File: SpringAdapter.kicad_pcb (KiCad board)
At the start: 2 copper layers, 81.7 x 26.6 mm, 50 parts, among them J1 Molex 0472861001, J2 Molex 0472861001, J3 Molex 0472861001, J4 Molex 0472861001, U1 XC6206P332MR-G, U3 GL852G-OHY60_C7501404, X1 12MHz

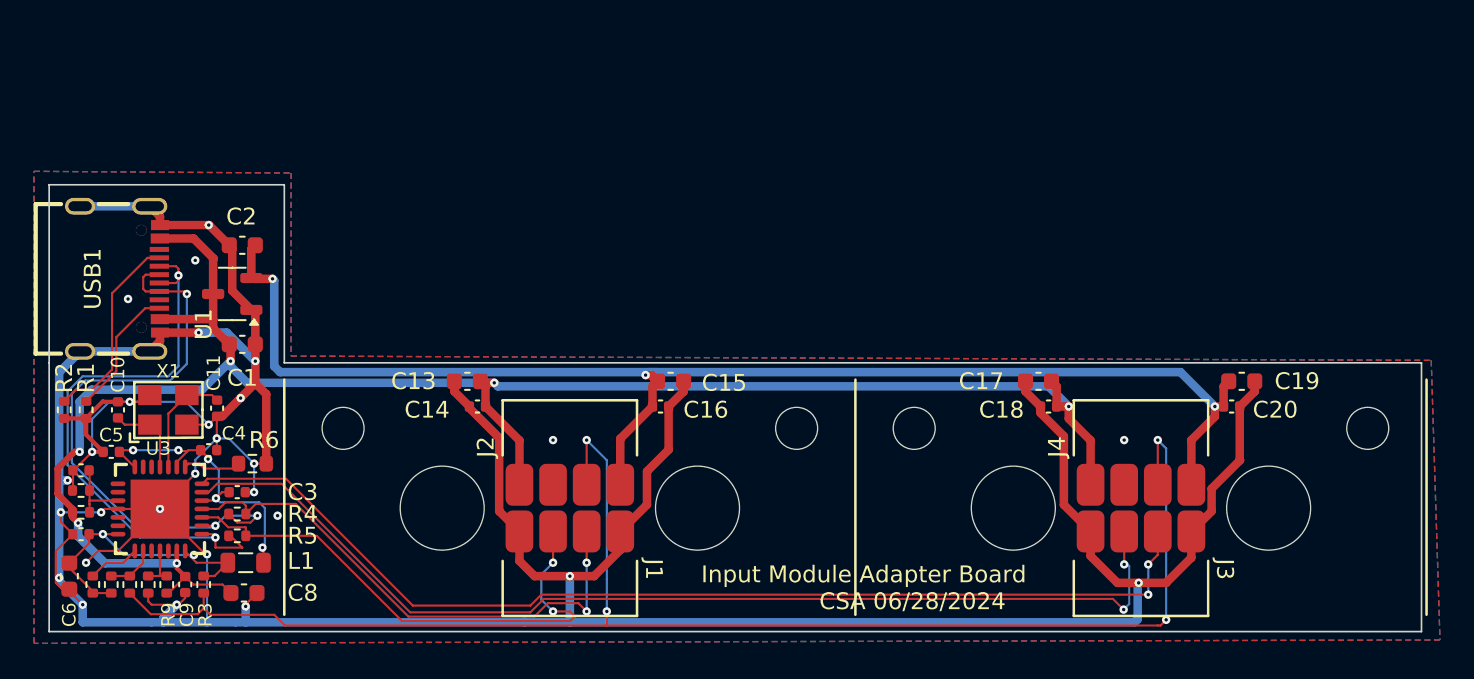
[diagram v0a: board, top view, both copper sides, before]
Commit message: Move USB-C adapter up 1mm
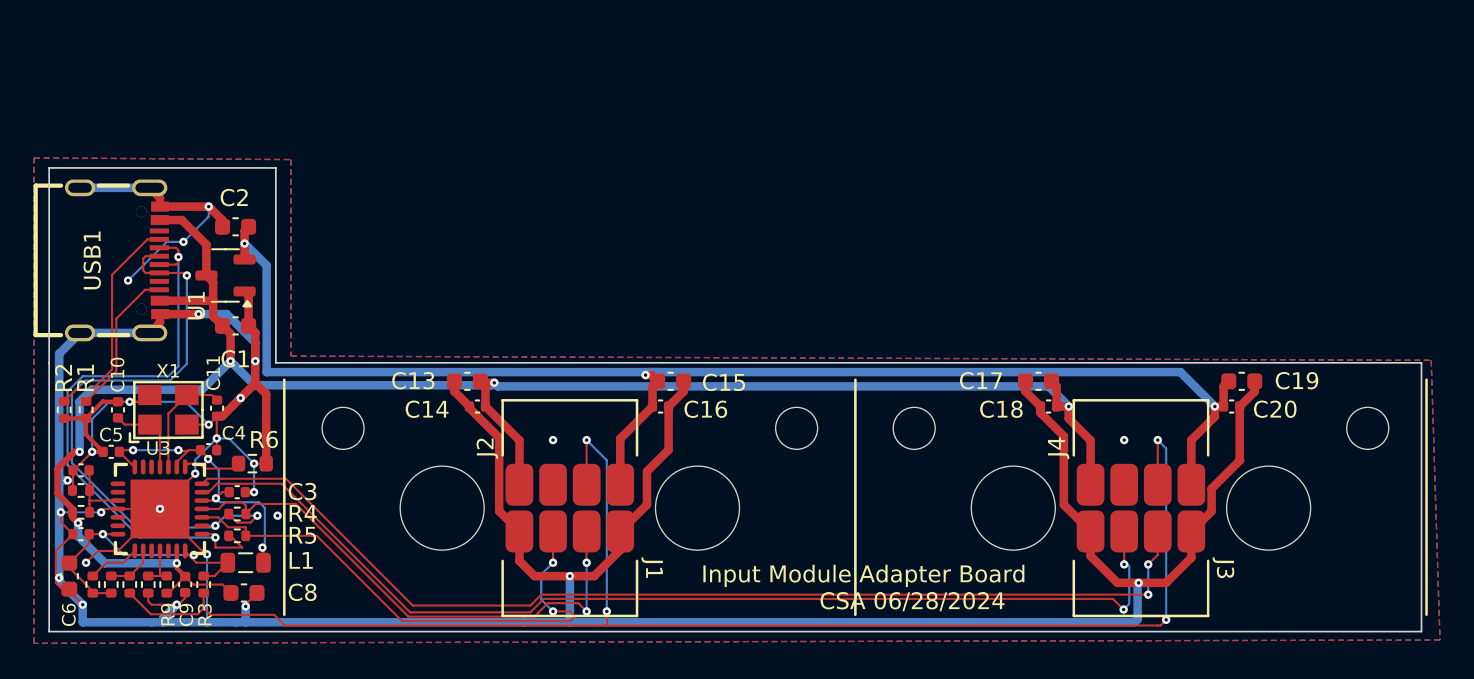
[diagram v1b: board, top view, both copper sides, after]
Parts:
- moved C1 1.17 mm to (96.1, 97.8)
- moved U1 1.17 mm to (95.5, 94.8)
- moved C2 1.17 mm to (96.1, 91.9)
- moved USB1 1.10 mm to (89.2, 93.9)
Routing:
- net GND: track 257.8 -> 263.7 mm
- net +3.3VP: track 81.7 -> 83.6 mm
- net /USB_D_P: track 36.1 -> 37.2 mm
- net /USB_D_N: track 34.9 -> 36.0 mm
- net Net-(USB1-CC1): track 11.9 -> 13.0 mm
- net Net-(USB1-CC2): track 7.84 -> 8.94 mm
- net +5V: track 112.3 -> 112.9 mm
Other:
- board size 81.7 x 26.6 mm -> 81.7 x 27.6 mm

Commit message: DFM work
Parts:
- added H10: Tooling Hole, ExternalMount:JLCPCB Tooling Hole, F.Cu at (86.1, 114.9)
- added H11: Tooling Hole, ExternalMount:JLCPCB Tooling Hole, F.Cu at (165.3, 101.4)
- added H12: Tooling Hole, ExternalMount:JLCPCB Tooling Hole, F.Cu at (165.2, 114.6)
- added H9: Tooling Hole, ExternalMount:JLCPCB Tooling Hole, F.Cu at (97.0, 89.8)
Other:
- board text added: "JLCJLCJLCJLC"

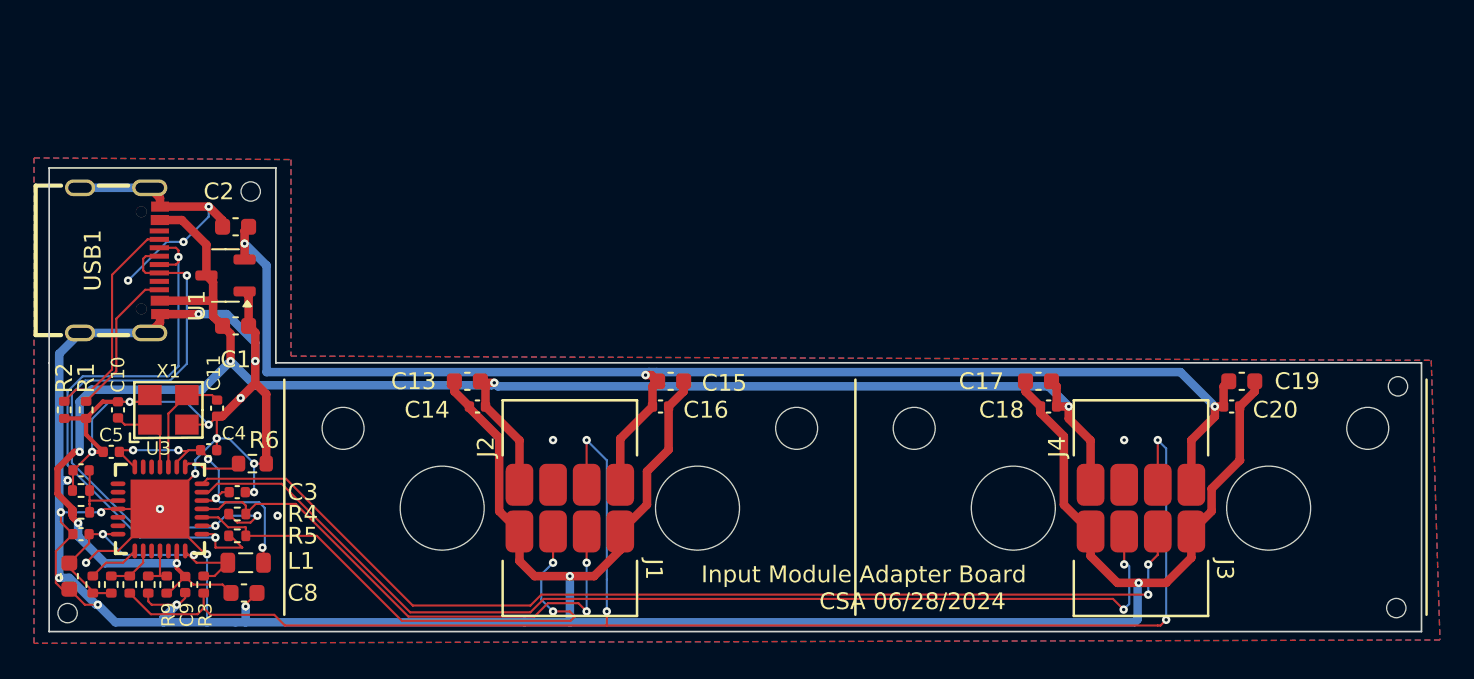
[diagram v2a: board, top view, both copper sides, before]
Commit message: Schematic/board v2: add CH32V003 to read board ID and control power/sleep
The microcontroller allows us to actually monitor the BOARD_ID and USB CC1/2
lines to monitor and control power consumption.  It uses the unused 3rd
USB port on the hub.  ESD protection has also been added to all touchable
connectors.  A programming connector for the CH32V003 has been added based
on the same molex 2mm-pitch spring connector we use for input modules.

CH32V003 USB interface based on
  https://github.com/cnlohr/rv003usb
and we expect to flash the USB bootloader on this to allow it to be
reprogrammed by the end user:
  https://github.com/cnlohr/rv003usb/tree/master/bootloader

FreeCAD model updated.  Switched to realthunder FreeCAD fork since
it handled the parametric dependency updates better.
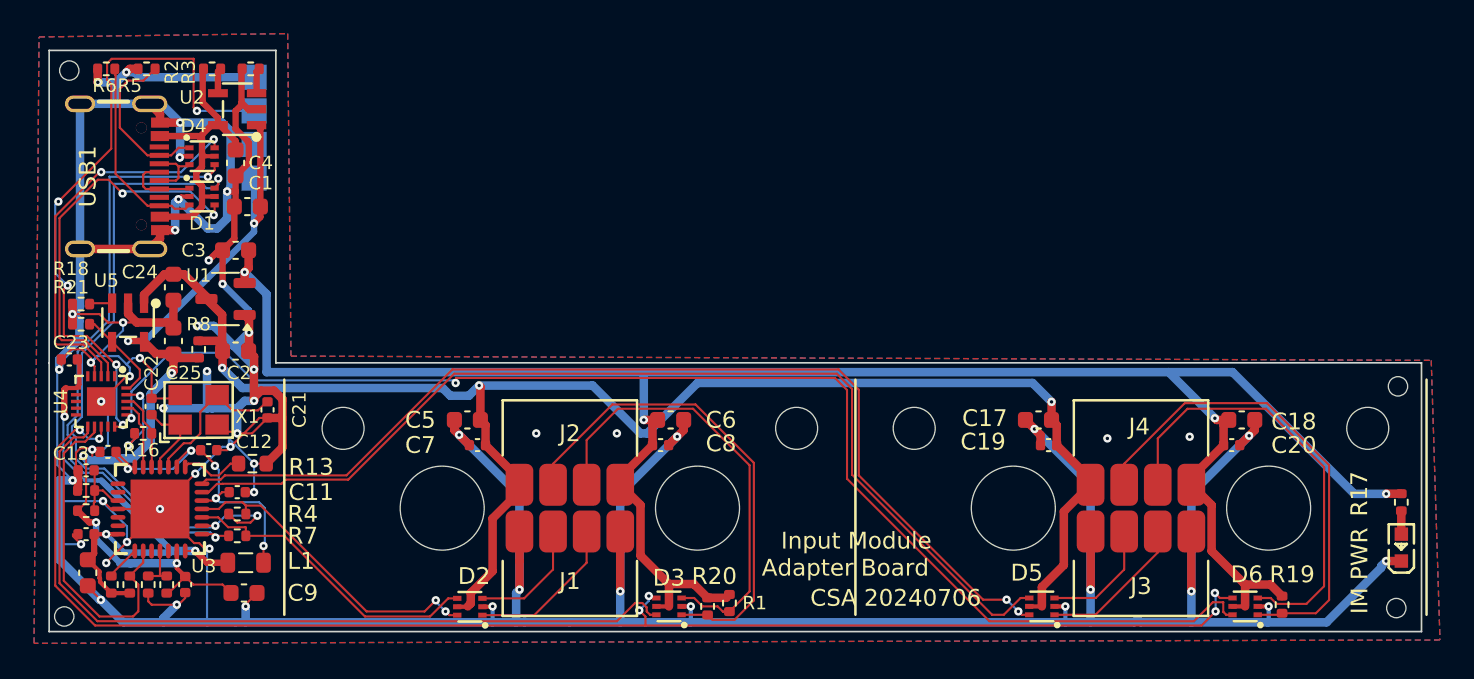
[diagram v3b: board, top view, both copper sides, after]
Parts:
- added C1: 10uF, Capacitor_SMD:C_0603_1608Metric, F.Cu at (96.8, 90.7)
- added C23: 100nF, Capacitor_SMD:C_0402_1005Metric, F.Cu at (86.2, 99.8)
- added C24: 10uF, Capacitor_SMD:C_0603_1608Metric, F.Cu at (92.4, 95.5)
- added C25: 10uF, Capacitor_SMD:C_0603_1608Metric, F.Cu at (92.4, 98.7)
- added C4: 10uF, Capacitor_SMD:C_0603_1608Metric, F.Cu at (96.1, 88.1)
- added D1: USBLC6-2P6_C2827693, ExternalMount:SOT-666-6_L1.6-W1.2-P0.50-LS1.6-BL, F.Cu at (94.1, 90.1)
- added D2: USBLC6-2P6_C2827693, ExternalMount:SOT-666-6_L1.6-W1.2-P0.50-LS1.6-BL, F.Cu at (110.0, 114.5)
- added D3: USBLC6-2P6_C2827693, ExternalMount:SOT-666-6_L1.6-W1.2-P0.50-LS1.6-BL, F.Cu at (121.9, 114.5)
- added D4: USBLC6-2P6_C2827693, ExternalMount:SOT-666-6_L1.6-W1.2-P0.50-LS1.6-BL, F.Cu at (94.1, 87.7)
- added D5: USBLC6-2P6_C2827693, ExternalMount:SOT-666-6_L1.6-W1.2-P0.50-LS1.6-BL, F.Cu at (144.1, 114.5)
- added D6: USBLC6-2P6_C2827693, ExternalMount:SOT-666-6_L1.6-W1.2-P0.50-LS1.6-BL, F.Cu at (156.2, 114.5)
- added LED1: Input Module Power, ExternalMount:LED0603-RD-YELLOW, F.Cu at (165.5, 111.0)
- added R16: 1.5k 5%, Resistor_SMD:R_0402_1005Metric, F.Cu at (90.6, 104.2)
- added R17: 330, Resistor_SMD:R_0402_1005Metric, F.Cu at (165.5, 108.3)
- added R18: 5.1k, Resistor_SMD:R_0402_1005Metric, F.Cu at (86.9, 96.5)
- added R19: 100k, Resistor_SMD:R_0402_1005Metric, F.Cu at (158.4, 114.4)
- added R2: 4.7k, Resistor_SMD:R_0402_1005Metric, F.Cu at (94.7, 82.5)
- added R20: 100k, Resistor_SMD:R_0402_1005Metric, F.Cu at (124.2, 114.5)
- added R3: 4.7k, Resistor_SMD:R_0402_1005Metric, F.Cu at (97.0, 82.5)
- added R8: 0, Resistor_SMD:R_0402_1005Metric, F.Cu at (93.9, 99.2)
- added TP1: 5V, TestPoint:TestPoint_Pad_1.5x1.5mm, B.Cu at (97.2, 89.0)
- added TP2: n/c, TestPoint:TestPoint_Pad_1.5x1.5mm, B.Cu at (97.2, 87.0)
- added TP3: SWIO, TestPoint:TestPoint_Pad_1.5x1.5mm, B.Cu at (97.2, 85.0)
- added TP4: GND, TestPoint:TestPoint_Pad_1.5x1.5mm, B.Cu at (97.2, 83.0)
- added U2: SY6280AAC, ExternalMount:SOT-23-5_L3.0-W1.7-P0.95-LS2.8-BL, F.Cu at (96.2, 84.9)
- added U4: CH32V003F4U6, ExternalMount:QFN-20_L3.0-W3.0-P0.40-TL-EP1.7, F.Cu at (88.1, 102.3)
- added U5: SY6280AAC, ExternalMount:SOT-23-5_L3.0-W1.7-P0.95-LS2.8-BL, F.Cu at (89.7, 97.6)
- H1, H2: footprint MountingHole:MountingHole_5mm -> ExternalMount:MountingHole_5mm_no_keepout
- H10: renamed from H6; footprint MountingHole:MountingHole_5mm -> ExternalMount:MountingHole_5mm_no_keepout
- H9: renamed from H5; footprint MountingHole:MountingHole_5mm -> ExternalMount:MountingHole_5mm_no_keepout
- R1: renamed from R3; value 5.1k -> 10k
- R21: renamed from R12; value 0 -> 100k
- moved R1 31.3 mm to (125.5, 114.3)
- moved R5 20.6 mm to (90.8, 82.5), turned to 180 degrees
- moved R6 20.5 mm to (88.4, 82.5), turned to 180 degrees
- moved R21 15.8 mm to (86.9, 97.7), turned to 180 degrees
- moved H5 13.0 mm to (86.2, 82.6)
- moved USB1 5.00 mm to (89.2, 88.9)
- moved C21 3.00 mm to (98.0, 102.8)
- moved C17 2.30 mm to (143.9, 103.4)
- moved C18 2.30 mm to (156.0, 103.4)
- moved C19 2.30 mm to (144.5, 104.9)
- moved C20 2.30 mm to (155.4, 104.9)
- moved C5 2.30 mm to (109.9, 103.4)
- moved C6 2.30 mm to (122.0, 103.4)
- moved C7 2.30 mm to (110.5, 104.9)
- moved C8 2.30 mm to (121.4, 104.9)
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- renumbered C9 to C10, C3 to C11, C4 to C12, C5 to C13, C6 to C14, C7 to C15, C12 to C16, C19 to C18, C18 to C19, C1 to C2, C11 to C21, C10 to C22, C2 to C3, C13 to C5, C15 to C6, C14 to C7, C16 to C8, C8 to C9, H7 to H11, H8 to H12, H9 to H5, H10 to H6, H11 to H7, H12 to H8, R8 to R10, R10 to R11, R7 to R12, R6 to R13, R13 to R14, R11 to R15, R1 to R5, R2 to R6, R5 to R7
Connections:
- C17 pad 1: +5V -> +5VP
- C19 pad 1: +5V -> +5VP
- C2 pad 1: +5V -> +5VP
- C5 pad 1: +5V -> +5VP
- C7 pad 1: +5V -> +5VP
- J1 pad 2: /USB_DM1 -> Net-(J1-Pin_2)
- J1 pad 3: /USB_DP1 -> Net-(J1-Pin_3)
- J2 pad 2: /~{SLEEP} -> /~{SLEEP1_UNP}
- J2 pad 3: unconnected-(J2-Pin_3-Pad3) -> /BOARD_ID1_UNP
- J2 pad 4: +5V -> +5VP
- J3 pad 2: /USB_DM2 -> Net-(J3-Pin_2)
- J3 pad 3: /USB_DP2 -> Net-(J3-Pin_3)
- J4 pad 2: /~{SLEEP} -> /~{SLEEP2_UNP}
- J4 pad 3: unconnected-(J4-Pin_3-Pad3) -> /BOARD_ID2_UNP
- J4 pad 4: +5V -> +5VP
- R1 pad 1: +3.3V -> +3.3VP
- R1 pad 2: /~{SLEEP} -> /~{SLEEP1_UNP}
- R15 pad 2: Net-(U3-PGANG) -> /PGANG
- R21 pad 1: Net-(U3-PGANG) -> /PWREN
- R21 pad 2: /~{SLEEP} -> GND
- R5 pad 1: Net-(USB1-CC2) -> /CC1_UNP
- R6 pad 1: Net-(USB1-CC1) -> /CC2_UNP
- U1 pad 3: +5V -> +5VP
- U3 pad 12: unconnected-(U3-DM3-Pad12) -> /USB_DM3
- U3 pad 13: unconnected-(U3-DP3-Pad13) -> /USB_DP3
- U3 pad 23: Net-(U3-PGANG) -> /PGANG
- USB1 pad A4B9: +5V -> V-UNFUSED
- USB1 pad A5: Net-(USB1-CC1) -> /CC1_UNP
- USB1 pad A6: /USB_D_P -> /USB_DP_UNP
- USB1 pad A7: /USB_D_N -> /USB_DN_UNP
- USB1 pad B4A9: +5V -> V-UNFUSED
- USB1 pad B5: Net-(USB1-CC2) -> /CC2_UNP
- USB1 pad B6: /USB_D_P -> /USB_DP_UNP
- USB1 pad B7: /USB_D_N -> /USB_DN_UNP
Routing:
- net GND: track 263.8 -> 372.8 mm, vias 28 -> 55
- net +5VP: track 0.00 -> 95.7 mm, vias 0 -> 3
- net /BOARD_ID2: track 0.00 -> 79.7 mm, vias 0 -> 2
- net +5V: track 112.9 -> 52.2 mm
- net /BOARD_ID1: track 0.00 -> 47.7 mm
- net +3.3VP: track 83.6 -> 122.1 mm, vias 3 -> 4
- net /SWIO: track 0.00 -> 38.1 mm, vias 0 -> 5
- net /BOARD_ID1_UNP: track 0.00 -> 29.2 mm
- net /BOARD_ID2_UNP: track 0.00 -> 29.1 mm
- net /~{SLEEP1_UNP}: track 0.00 -> 26.9 mm
- net /~{SLEEP2_UNP}: track 0.00 -> 26.5 mm
- net /CC1: track 0.00 -> 23.5 mm, vias 0 -> 2
- net /CC2: track 0.00 -> 23.1 mm, vias 0 -> 2
- net /PGANG: track 0.00 -> 19.9 mm
- net V-UNFUSED: track 0.00 -> 18.4 mm
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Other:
- board size 81.7 x 27.6 mm -> 81.7 x 34.6 mm
- board text added: "CSA 20240706"
- board text added: "IM PWR"
- board text added: "Moved USB connector -5mm in Y direction Board edge moved -7mm in Y direction"
- board text removed: "CSA 06/28/2024"
